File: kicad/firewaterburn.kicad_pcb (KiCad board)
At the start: 4 copper layers, 70 x 40 mm, 110 parts, among them J201 AudioJack2_SwitchT, J202 AudioJack2_SwitchT, J203 AudioJack2_SwitchT, J204 AudioJack2_SwitchT, J205 AudioJack2_SwitchT, J206 AudioJack2_SwitchT, J301 Conn_ARM_SWD_TagConnect_TC2030, J303 Conn_02x10_Odd_Even, J501 EA W128064-XALG, J601 Conn_Coaxial, J701 Conn_01x03, P101 USB_C_Plug_USB2.0, Q401 SI7421DN-T1-E3, Q701 SI7421DN-T1-E3, Q702 DMN61D9UWQ-13, U101 TPD4E02B04DQA, U301 BL654, U401 LT3973-3.3, U402 STUSB4500QTR, U403 LM2775DSG, U501 MIC2290, U601 NRF7002-QFAA-Rx, Y301 Crystal, Y601 40MHz

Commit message: new board
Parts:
- removed TP402, TP403, TP404, TP405: TestPoint, TestPoint:TestPoint_Keystone_5015_Micro-Minature
- added C306: 100nF, Capacitor_SMD:C_0603_1608Metric, F.Cu at (142.7, 77.5)
- added R304: 47k, Resistor_SMD:R_0603_1608Metric, F.Cu at (144.3, 77.5)
- added R306: 330, Resistor_SMD:R_0603_1608Metric, F.Cu at (145.9, 77.5)
- added SW301: SW_Push, Button_Switch_SMD:SW_Push_SPST_NO_Alps_SKRK, F.Cu at (144.3, 80.8)
- added U603: TCK106AF, mylib_ic:SOT-25, F.Cu at (142.0, 96.5)
- J501: footprint mylib_connector:SFV31R-4STE1HLF -> mylib_connector:F32R-1A7H1-11031
- moved C501 6.78 mm to (106.0, 96.2), turned to 0 degrees
- moved R406 6.15 mm to (109.1, 91.7), turned to 90 degrees
- moved J501 6.00 mm to (135.0, 73.0)
- moved Q702 5.51 mm to (149.7, 77.2)
- moved R703 5.48 mm to (149.7, 74.7)
- moved R701 5.41 mm to (151.8, 77.4)
- moved Q701 5.29 mm to (154.7, 77.2)
- moved C502 5.17 mm to (103.0, 91.0), turned to 180 degrees
- moved C404 4.74 mm to (115.2, 90.5), turned to 90 degrees
- moved C402 4.57 mm to (109.1, 88.4), turned to 90 degrees
- moved C405 4.51 mm to (115.2, 87.4), turned to -90 degrees
- moved R502 4.47 mm to (105.4, 91.0), turned to 180 degrees
- moved L501 4.14 mm to (102.8, 94.2), turned to 90 degrees
- moved U401 3.91 mm to (112.2, 91.6), turned to 180 degrees
- moved C505 3.87 mm to (133.0, 79.0), turned to 0 degrees
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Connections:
- net /mcu_n_tft/SWCLK renamed /mcu/SWCLK
- net /mcu_n_tft/SWDIO renamed /mcu/SWDIO
- net /mcu_n_tft/SWO renamed /mcu/SWO
- net /mcu_n_tft/XL1 renamed /mcu/XL1
- net /mcu_n_tft/XL2 renamed /mcu/XL2
- net /mcu_n_tft/~{Reset} renamed /mcu/~{MCU_RESET}
- C601 pad 1: +3V3 -> IOVDD
- J201 pad T: /OUTPUT/probe0 -> /analog/probe0
- J202 pad T: /OUTPUT/probe1 -> /analog/probe1
- J203 pad T: /OUTPUT/probe2 -> /analog/probe2
- J204 pad T: /OUTPUT/probe3 -> /analog/probe3
- J205 pad T: /OUTPUT/probe4 -> /analog/probe4
- J206 pad T: /OUTPUT/probe5 -> /analog/probe5
- J303 pad 1: /mcu_n_tft/UART_TX -> /mcu/UART_TX
- J303 pad 10: /mcu_n_tft/QSPI_IO2 -> /mcu/TFT_D/C
- J303 pad 11: unconnected-(J303-Pin_11-Pad11) -> /mcu/QSPI_IO2
- J303 pad 12: /mcu_n_tft/QSPI_IO3 -> /mcu/QSPI_CLK
- J303 pad 13: unconnected-(J303-Pin_13-Pad13) -> /mcu/QSPI_IO1
- J303 pad 14: unconnected-(J303-Pin_14-Pad14) -> /mcu/QSPI_~{CS}
- J303 pad 15: unconnected-(J303-Pin_15-Pad15) -> /mcu/QSPI_IO0
- J303 pad 19: unconnected-(J303-Pin_19-Pad19) -> +3V3
- J303 pad 2: /mcu_n_tft/UART_RX -> /mcu/UART_RX
- J303 pad 20: unconnected-(J303-Pin_20-Pad20) -> GND
- J303 pad 3: /mcu_n_tft/SDA -> /mcu/SCL
- J303 pad 4: /mcu_n_tft/SCL -> /mcu/SDA
- J303 pad 5: /mcu_n_tft/QSPI_CLK -> /mcu/TFT_~{CS}
- J303 pad 6: /mcu_n_tft/QSPI_IO0 -> /mcu/TFT_MOSI
- J303 pad 7: /mcu_n_tft/QSPI_~{CS} -> /mcu/TFT_~{RESET}
- J303 pad 8: /mcu_n_tft/QSPI_IO1 -> /mcu/TFT_CLK
- J303 pad 9: unconnected-(J303-Pin_9-Pad9) -> /mcu/QSPI_IO3
- J501 pad 15: /mcu_n_tft/TFT_~{CS} -> /mcu/TFT_~{CS}
- J501 pad 16: /mcu_n_tft/TFT_~{RESET} -> /mcu/TFT_~{RESET}
- J501 pad 17: /mcu_n_tft/TFT_D/C -> /mcu/TFT_D/C
- J501 pad 20: /mcu_n_tft/TFT_CLK -> /mcu/TFT_CLK
- J501 pad 21: /mcu_n_tft/TFT_MOSI -> /mcu/TFT_MOSI
- R101 pad 2: /mcu_n_tft/SDA -> /mcu/SDA
- R102 pad 2: /mcu_n_tft/SCL -> /mcu/SCL
- R103 pad 2: /mcu_n_tft/I2C_INT -> /mcu/I2C_INT
- R201 pad 2: /OUTPUT/probe0 -> /analog/probe0
- R202 pad 2: /OUTPUT/probe1 -> /analog/probe1
- R203 pad 2: /OUTPUT/probe2 -> /analog/probe2
- R204 pad 2: /OUTPUT/probe3 -> /analog/probe3
- R205 pad 1: /OUTPUT/probe0 -> /analog/probe0
- R206 pad 1: /OUTPUT/probe1 -> /analog/probe1
- R207 pad 1: /OUTPUT/probe2 -> /analog/probe2
- R208 pad 1: /OUTPUT/probe3 -> /analog/probe3
- R209 pad 2: /OUTPUT/probe4 -> /analog/probe4
- R210 pad 2: /OUTPUT/probe5 -> /analog/probe5
- R213 pad 1: /OUTPUT/probe4 -> /analog/probe4
- R214 pad 1: /OUTPUT/probe5 -> /analog/probe5
- R302 pad 2: /mcu_n_tft/LED1 -> /mcu/LED1
- R303 pad 2: /mcu_n_tft/LED2 -> /mcu/LED2
- U301 pad 10: /mcu_n_tft/COEX_REQ -> /mcu/COEX_STATUS
- U301 pad 11: /mcu_n_tft/QSPI_IO1 -> /mcu/SDA
- U301 pad 12: /mcu_n_tft/COEX_STATUS -> /mcu/TFT_~{CS}
- U301 pad 13: /mcu_n_tft/QSPI_CLK -> /mcu/SCL
- U301 pad 14: /mcu_n_tft/BUCKEN -> /mcu/TFT_~{RESET}
- U301 pad 16: /mcu_n_tft/QSPI_IO2 -> /mcu/TFT_D/C
- U301 pad 18: /mcu_n_tft/QSPI_IO3 -> /mcu/TFT_CLK
- U301 pad 2: unconnected-(U301-P1.04-Pad2) -> /mcu/BUCKEN
- U301 pad 20: /mcu_n_tft/COEX_GRANT -> /mcu/TFT_MOSI
- U301 pad 21: unconnected-(U301-P0.16-Pad21) -> /mcu/I2C_INT
- U301 pad 22: /mcu_n_tft/SW_CTRL1 -> unconnected-(U301-P0.14-Pad22)
- U301 pad 34: /OUTPUT/probe4 -> unconnected-(U301-P0.04/AIN2-Pad34)
- U301 pad 35: /fan_control/PWM -> /fan_control/TACHO
- U301 pad 36: unconnected-(U301-P0.26-Pad36) -> /mcu/UART_RX
- U301 pad 37: /fan_control/TACHO -> /fan_control/PWM
- U301 pad 38: unconnected-(U301-P0.27-Pad38) -> /mcu/UART_TX
- U301 pad 39: /OUTPUT/probe5 -> /analog/probe0
- U301 pad 4: unconnected-(U301-P1.02-Pad4) -> /mcu/IRQ
- U301 pad 44: /OUTPUT/probe7 -> /analog/probe1
- U301 pad 45: /OUTPUT/probe3 -> /analog/probe5
- U301 pad 46: /OUTPUT/probe6 -> /analog/probe2
- U301 pad 48: /OUTPUT/probe1 -> /analog/probe3
- U301 pad 49: /OUTPUT/probe2 -> /mcu/QSPI_CLK
- U301 pad 5: unconnected-(U301-P1.03-Pad5) -> /mcu/SW_CTRL1
- U301 pad 50: /OUTPUT/probe0 -> /analog/probe4
- U301 pad 51: /mcu_n_tft/SCL -> /mcu/QSPI_IO0
- U301 pad 53: /mcu_n_tft/SDA -> /mcu/QSPI_IO1
- U301 pad 54: /mcu_n_tft/I2C_INT -> /mcu/QSPI_IO2
- U301 pad 56: unconnected-(U301-P1.13-Pad56) -> /mcu/QSPI_IO3
- U301 pad 6: unconnected-(U301-P1.01-Pad6) -> /mcu/COEX_GRANT
- U301 pad 60: /mcu_n_tft/BUTTON1 -> /mcu/QSPI_~{CS}
- U301 pad 61: /mcu_n_tft/IRQ -> /mcu/BUTTON
- U301 pad 62: /mcu_n_tft/BUTTON2 -> /mcu/LED1
- U301 pad 63: /mcu_n_tft/LED2 -> /mcu/WIFI_ENABLE
- U301 pad 64: /mcu_n_tft/LED1 -> /mcu/LED2
- U301 pad 8: /mcu_n_tft/QSPI_~{CS} -> /mcu/COEX_REQ
- U301 pad 9: /mcu_n_tft/QSPI_IO0 -> unconnected-(U301-P0.23-Pad9)
- U402 pad 19: /mcu_n_tft/I2C_INT -> /mcu/I2C_INT
- U402 pad 7: /mcu_n_tft/SCL -> /mcu/SCL
- U402 pad 8: /mcu_n_tft/SDA -> /mcu/SDA
- U601 pad 30: /mcu_n_tft/BUCKEN -> /mcu/BUCKEN
- U601 pad 35: /mcu_n_tft/QSPI_CLK -> /mcu/QSPI_CLK
- U601 pad 36: /mcu_n_tft/QSPI_~{CS} -> /mcu/QSPI_~{CS}
- U601 pad 37: /mcu_n_tft/QSPI_IO0 -> /mcu/QSPI_IO0
- U601 pad 38: /mcu_n_tft/QSPI_IO1 -> /mcu/QSPI_IO1
- U601 pad 39: /mcu_n_tft/QSPI_IO3 -> /mcu/QSPI_IO2
- U601 pad 40: /mcu_n_tft/QSPI_IO2 -> /mcu/QSPI_IO3
- U601 pad 41: /mcu_n_tft/COEX_STATUS -> /mcu/COEX_STATUS
- U601 pad 42: /mcu_n_tft/COEX_REQ -> /mcu/COEX_REQ
- U601 pad 43: /mcu_n_tft/COEX_GRANT -> /mcu/COEX_GRANT
- U601 pad 45: /mcu_n_tft/SW_CTRL1 -> /mcu/SW_CTRL1
- U601 pad 46: /mcu_n_tft/IRQ -> /mcu/IRQ
- U601 pad 48: +3V3 -> IOVDD
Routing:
- net GND: track 51.8 -> 288.9 mm, vias 2 -> 199
- net +3V3: track 48.1 -> 180.8 mm, vias 11 -> 36
- net /mcu/TFT_D/C: track 0.00 -> 68.6 mm, vias 0 -> 3
- net /mcu/TFT_CLK: track 0.00 -> 68.2 mm, vias 0 -> 3
- net /mcu/TFT_MOSI: track 0.00 -> 67.8 mm, vias 0 -> 3
- net /mcu/TFT_~{RESET}: track 0.00 -> 67.4 mm, vias 0 -> 3
- net /mcu/SCL: track 0.00 -> 67.1 mm, vias 0 -> 5
- net /mcu/SDA: track 0.00 -> 67.1 mm, vias 0 -> 5
- net /mcu/TFT_~{CS}: track 0.00 -> 66.8 mm, vias 0 -> 3
- net VDD: track 3.40 -> 59.5 mm, vias 0 -> 10
- net /mcu/QSPI_~{CS}: track 0.00 -> 55.7 mm, vias 0 -> 3
- net /analog/probe0: track 0.00 -> 51.6 mm, vias 0 -> 3
- net /mcu/QSPI_CLK: track 0.00 -> 49.2 mm, vias 0 -> 2
- net /analog/probe1: track 0.00 -> 44.6 mm, vias 0 -> 3
- net +12L: track 5.96 -> 50.2 mm
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- added copper zone on F.Cu, net +12L
- added copper zone on F.Cu, net +3V3
- added copper zone on F.Cu, net Net-(J701-Pin_2)
- added copper zone on F.Cu, net Net-(U501-SW)
- added copper zone on F.Cu, net VBUS
- added copper zone on In2.Cu, net VBUS
- added copper zone on F.Cu, net VDD
- added copper zone on In2.Cu, net VDD
- added copper zone on F.Cu, net VDD_BUCK
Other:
- board text added: "+3V3"
- board text added: "1"
- board text added: "GND"
- board text added: "QSPIO_CLK"
- board text added: "QSPIO_IO0"
- board text added: "QSPIO_IO1"
- board text added: "QSPIO_IO2"
- board text added: "QSPIO_IO3"
- board text added: "QSPI_~{CS}"
- board text added: "SCL"
- board text added: "SDA"
- board text added: "TFT_CLK"
- board text added: "TFT_D/C"
- board text added: "TFT_MOSI"
- board text added: "TFT_~{CS}"
- board text added: "TFT_~{RESET}"
- board text added: "UART RX"
- board text added: "UART TX"
- board text added: "X"
- board text removed: "ABC"

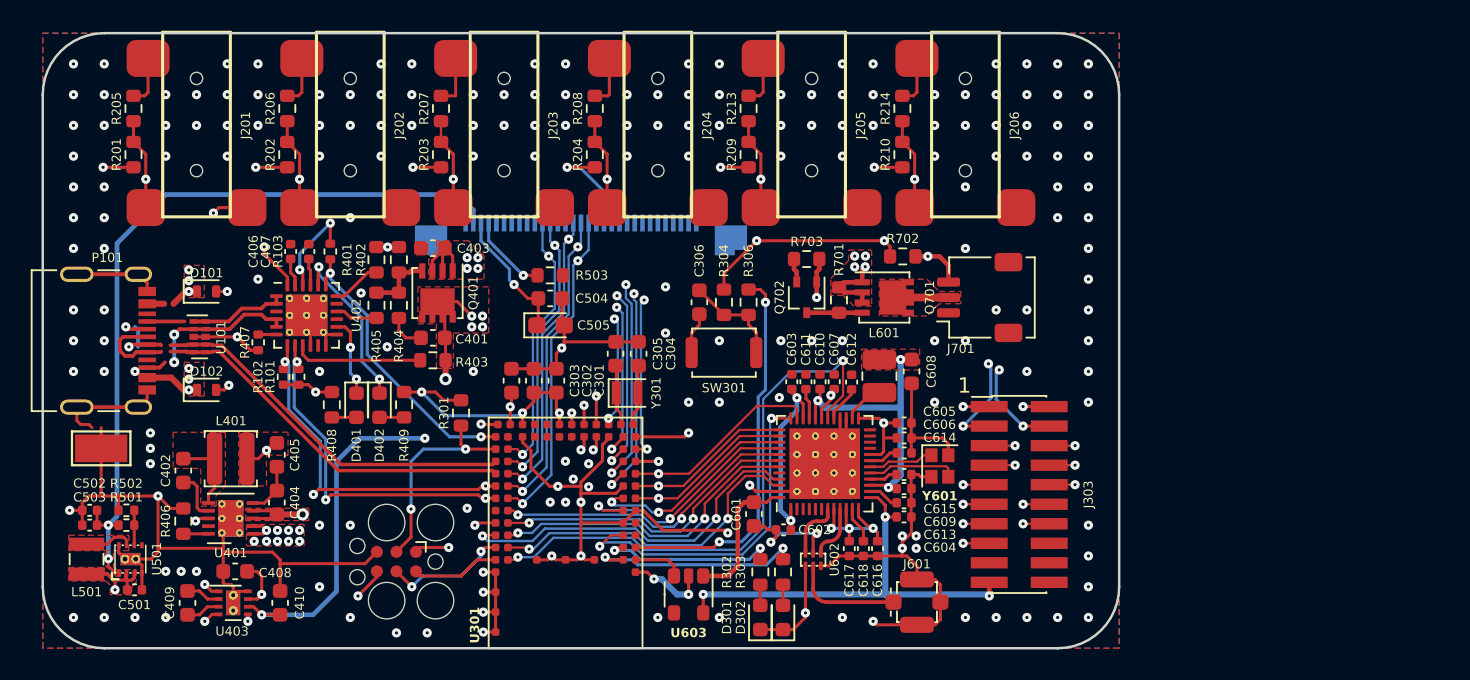
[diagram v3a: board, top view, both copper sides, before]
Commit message: upgrade 2 KiCAD 8.0
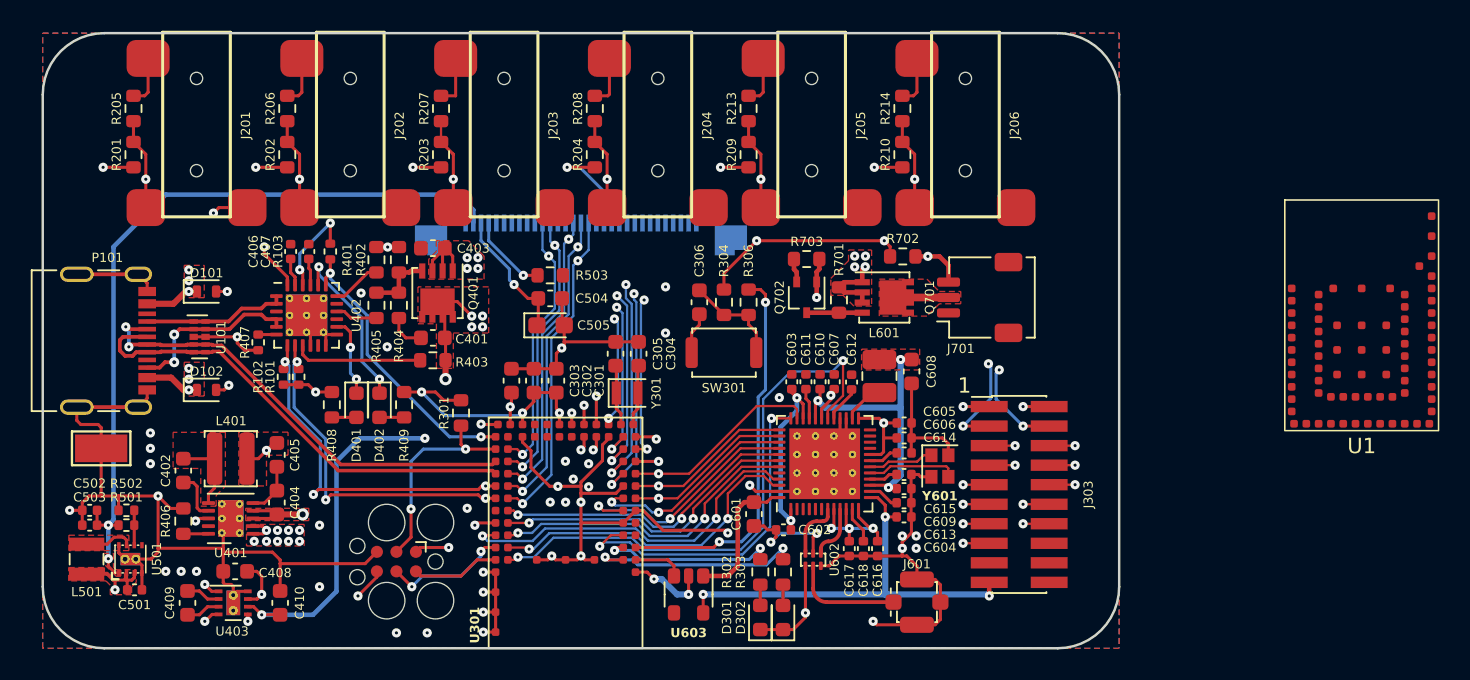
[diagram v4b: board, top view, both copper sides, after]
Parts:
- added U1: ~, mylib_ic:BL5340, F.Cu at (185.8, 78.3)
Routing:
- net VBUS: track 40.9 -> 43.0 mm
- net /pwr_supply/CC2: track 10.9 -> 11.5 mm
- net /pwr_supply/CC1: track 8.78 -> 9.38 mm
- net /D+: track 30.0 -> 30.6 mm
- net /D-: track 29.5 -> 30.1 mm
- net GND: track 288.9 -> 288.6 mm, vias 199 -> 53
